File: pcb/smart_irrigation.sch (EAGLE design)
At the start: 31 parts, among them IC1 TMP36, IC2 7805DT, IC3 7833DT, IC4 DS1307, Q1 IRF730, Q2 32.768, Q3 2N3904, U1 BL600

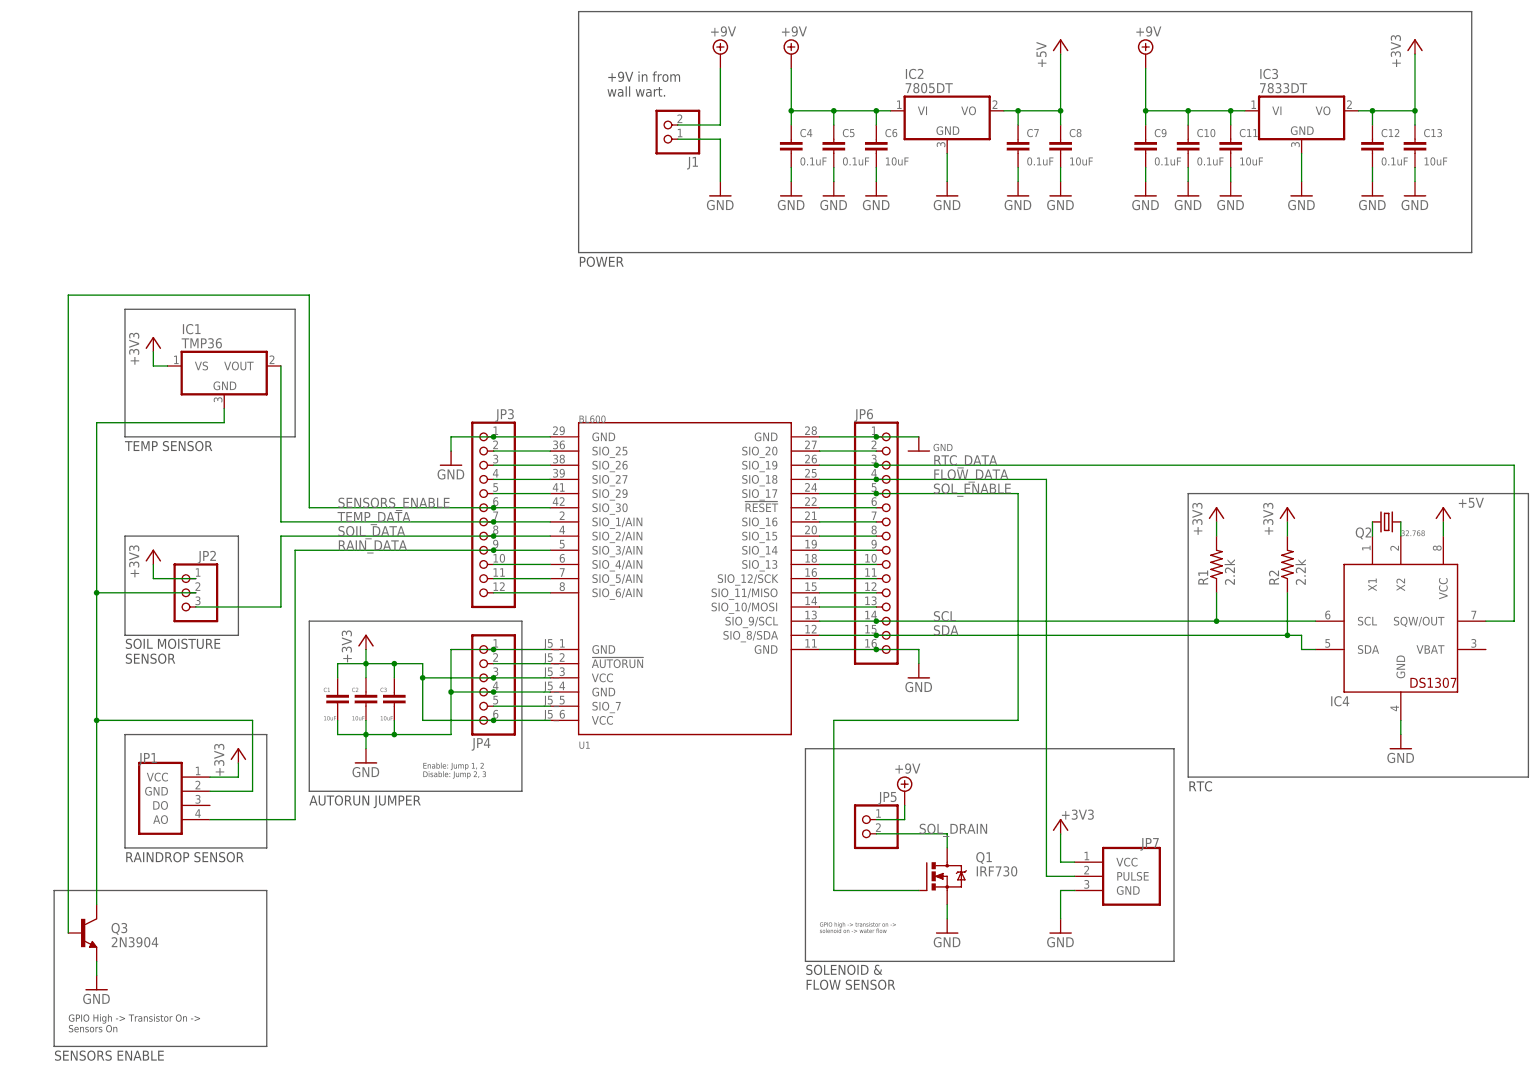
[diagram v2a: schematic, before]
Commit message: PCB: Change flow sensor GPIO pin
The flow sensor's pin was on the opposite side of the other sensors,
making for awkward routing.
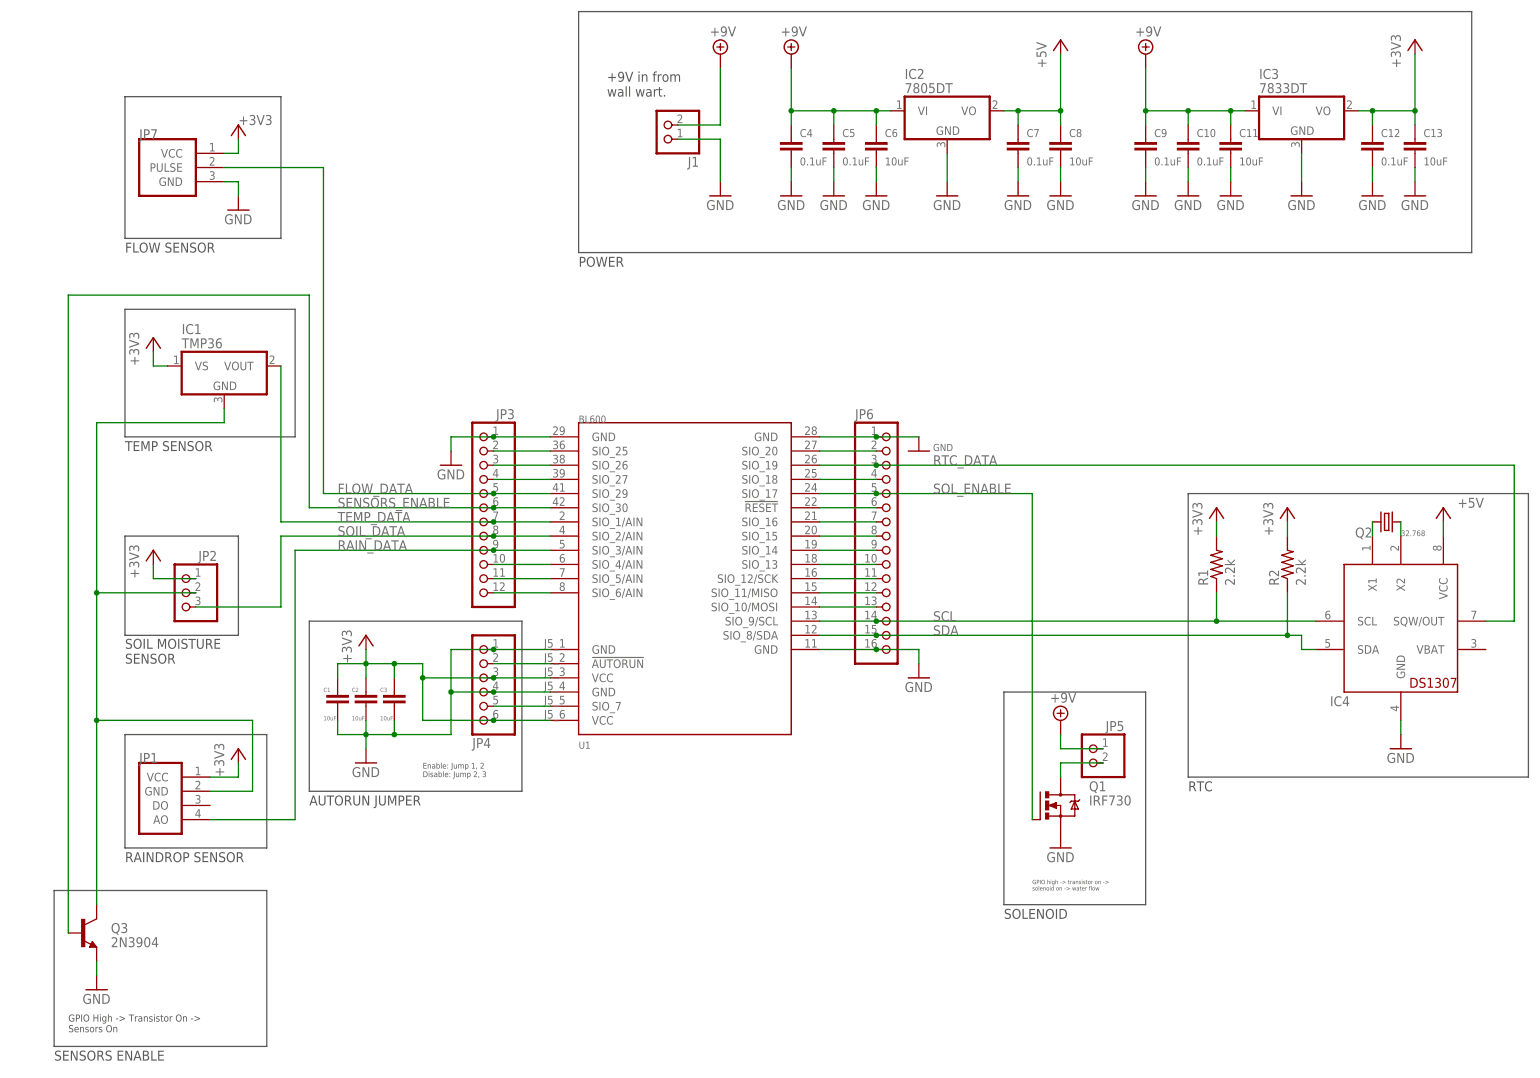
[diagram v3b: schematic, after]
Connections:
- removed net SIO_29: JP3.5, U1.SIO_29
- new net SIO_18: JP6.4, U1.SIO_18
- net FLOW_DATA: now also JP3.5, U1.SIO_29; no longer JP6.4, U1.SIO_18
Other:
- note added: "FLOW SENSOR"
- note added: "SOLENOID"
- note removed: "SOLENOID & FLOW SENSOR"
- moved on the sheet: JP5, JP7, Q1
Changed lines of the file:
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@@
 <setting verticaltext="up"/>
 </settings>
-<grid distance="0.1" unitdist="inch" unit="inch" style="lines" multiple="1" display="no" altdistance="0.01" altunitdist="inch" altunit="inch"/>
+<grid distance="0.1" unitdist="inch" unit="inch" style="lines" multiple="1" display="yes" altdistance="0.01" altunitdist="inch" altunit="inch"/>
 <layers>
 <layer number="1" name="Top" color="4" fill="1" visible="no" active="no"/>
@@
 <wire x1="93.98" y1="68.58" x2="55.88" y2="68.58" width="0.1524" layer="97"/>
 <wire x1="55.88" y1="68.58" x2="55.88" y2="99.06" width="0.1524" layer="97"/>
-<wire x1="144.78" y1="38.1" x2="144.78" y2="76.2" width="0.1524" layer="97"/>
-<wire x1="144.78" y1="76.2" x2="210.82" y2="76.2" width="0.1524" layer="97"/>
-<wire x1="210.82" y1="76.2" x2="210.82" y2="38.1" width="0.1524" layer="97"/>
-<wire x1="210.82" y1="38.1" x2="144.78" y2="38.1" width="0.1524" layer="97"/>
-<text x="144.78" y="33.02" size="1.778" layer="97">SOLENOID &amp;
-FLOW SENSOR</text>
-<text x="147.32" y="43.18" size="0.762" layer="97">GPIO high -&gt; transistor on -&gt;
+<wire x1="180.34" y1="48.26" x2="180.34" y2="86.36" width="0.1524" layer="97"/>
+<wire x1="180.34" y1="86.36" x2="205.74" y2="86.36" width="0.1524" layer="97"/>
+<wire x1="205.74" y1="86.36" x2="205.74" y2="48.26" width="0.1524" layer="97"/>
+<wire x1="205.74" y1="48.26" x2="180.34" y2="48.26" width="0.1524" layer="97"/>
+<text x="180.34" y="45.72" size="1.778" layer="97">SOLENOID</text>
+<text x="185.42" y="50.8" size="0.762" layer="97">GPIO high -&gt; transistor on -&gt;
 solenoid on -&gt; water flow</text>
 <wire x1="10.16" y1="50.8" x2="48.26" y2="50.8" width="0.1524" layer="97"/>
@@
 <text x="12.7" y="25.4" size="1.27" layer="97">GPIO High -&gt; Transistor On -&gt;
 Sensors On</text>
+<wire x1="22.86" y1="193.04" x2="50.8" y2="193.04" width="0.1524" layer="97"/>
+<wire x1="50.8" y1="193.04" x2="50.8" y2="167.64" width="0.1524" layer="97"/>
+<wire x1="50.8" y1="167.64" x2="22.86" y2="167.64" width="0.1524" layer="97"/>
+<wire x1="22.86" y1="167.64" x2="22.86" y2="193.04" width="0.1524" layer="97"/>
+<text x="22.86" y="165.1" size="1.778" layer="97">FLOW SENSOR</text>
 </plain>
 <instances>
@@
 <attribute name="VALUE" x="68.58" y="81.28" size="0.762" layer="96"/>
 </instance>
-<instance part="JP7" gate="A" x="200.66" y="53.34" rot="MR0"/>
-<instance part="+3V35" gate="G$1" x="190.5" y="63.5" smashed="yes">
-<attribute name="VALUE" x="190.5" y="63.5" size="1.778" layer="96"/>
-</instance>
-<instance part="GND14" gate="1" x="190.5" y="43.18"/>
-<instance part="Q1" gate="G$1" x="167.64" y="53.34"/>
-<instance part="JP5" gate="G$1" x="154.94" y="60.96" rot="MR0"/>
-<instance part="SUPPLY3" gate="G$1" x="162.56" y="68.58"/>
-<instance part="GND9" gate="1" x="170.18" y="43.18"/>
+<instance part="JP7" gate="A" x="33.02" y="180.34"/>
+<instance part="+3V35" gate="G$1" x="43.18" y="187.96" smashed="yes">
+<attribute name="VALUE" x="43.18" y="187.96" size="1.778" layer="96"/>
+</instance>
+<instance part="GND14" gate="1" x="43.18" y="172.72"/>
+<instance part="Q1" gate="G$1" x="187.96" y="66.04"/>
+<instance part="JP5" gate="G$1" x="195.58" y="73.66" rot="MR0"/>
+<instance part="SUPPLY3" gate="G$1" x="190.5" y="81.28"/>
+<instance part="GND9" gate="1" x="190.5" y="58.42"/>
 <instance part="Q3" gate="G1" x="15.24" y="43.18" smashed="yes">
 <attribute name="NAME" x="20.32" y="43.18" size="1.778" layer="95"/>
@@
 <pinref part="JP7" gate="A" pin="GND"/>
 <pinref part="GND14" gate="1" pin="GND"/>
-<wire x1="193.04" y1="50.8" x2="190.5" y2="50.8" width="0.1524" layer="91"/>
-<wire x1="190.5" y1="50.8" x2="190.5" y2="45.72" width="0.1524" layer="91"/>
+<wire x1="40.64" y1="177.8" x2="43.18" y2="177.8" width="0.1524" layer="91"/>
+<wire x1="43.18" y1="177.8" x2="43.18" y2="175.26" width="0.1524" layer="91"/>
 </segment>
 <segment>
 <pinref part="GND9" gate="1" pin="GND"/>
 <pinref part="Q1" gate="G$1" pin="S"/>
-<wire x1="170.18" y1="45.72" x2="170.18" y2="48.26" width="0.1524" layer="91"/>
 </segment>
 <segment>
@@
 <segment>
 <pinref part="SUPPLY3" gate="G$1" pin="+9V"/>
-<wire x1="162.56" y1="66.04" x2="162.56" y2="63.5" width="0.1524" layer="91"/>
+<wire x1="190.5" y1="78.74" x2="190.5" y2="76.2" width="0.1524" layer="91"/>
 <pinref part="JP5" gate="G$1" pin="1"/>
-<wire x1="162.56" y1="63.5" x2="157.48" y2="63.5" width="0.1524" layer="91"/>
+<wire x1="190.5" y1="76.2" x2="198.12" y2="76.2" width="0.1524" layer="91"/>
 </segment>
 </net>
@@
 <segment>
 <pinref part="+3V35" gate="G$1" pin="+3V3"/>
-<wire x1="190.5" y1="60.96" x2="190.5" y2="55.88" width="0.1524" layer="91"/>
+<wire x1="43.18" y1="185.42" x2="43.18" y2="182.88" width="0.1524" layer="91"/>
 <pinref part="JP7" gate="A" pin="VCC"/>
-<wire x1="190.5" y1="55.88" x2="193.04" y2="55.88" width="0.1524" layer="91"/>
+<wire x1="43.18" y1="182.88" x2="40.64" y2="182.88" width="0.1524" layer="91"/>
 </segment>
 </net>
@@
 </segment>
 </net>
-<net name="SIO_29" class="0">
+<net name="FLOW_DATA" class="0">
 <segment>
 <pinref part="U1" gate="G$1" pin="SIO_29"/>
 <pinref part="JP3" gate="G$1" pin="5"/>
 <wire x1="99.06" y1="121.92" x2="88.9" y2="121.92" width="0.1524" layer="91"/>
+<pinref part="JP7" gate="A" pin="PULSE"/>
+<wire x1="40.64" y1="180.34" x2="58.42" y2="180.34" width="0.1524" layer="91"/>
+<wire x1="58.42" y1="180.34" x2="58.42" y2="121.92" width="0.1524" layer="91"/>
+<wire x1="58.42" y1="121.92" x2="88.9" y2="121.92" width="0.1524" layer="91"/>
+<junction x="88.9" y="121.92"/>
+<label x="60.96" y="121.92" size="1.778" layer="95"/>
 </segment>
 </net>
@@
 </segment>
 </net>
-<net name="FLOW_DATA" class="0">
-<segment>
-<pinref part="JP6" gate="A" pin="4"/>
-<pinref part="U1" gate="G$1" pin="SIO_18"/>
-<wire x1="157.48" y1="124.46" x2="147.32" y2="124.46" width="0.1524" layer="91"/>
-<pinref part="JP7" gate="A" pin="PULSE"/>
-<wire x1="193.04" y1="53.34" x2="187.96" y2="53.34" width="0.1524" layer="91"/>
-<wire x1="187.96" y1="53.34" x2="187.96" y2="124.46" width="0.1524" layer="91"/>
-<wire x1="187.96" y1="124.46" x2="157.48" y2="124.46" width="0.1524" layer="91"/>
-<junction x="157.48" y="124.46"/>
-<label x="167.64" y="124.46" size="1.778" layer="95"/>
-</segment>
-</net>
 <net name="SOL_ENABLE" class="0">
 <segment>
@@
 <pinref part="JP6" gate="A" pin="5"/>
 <wire x1="147.32" y1="121.92" x2="157.48" y2="121.92" width="0.1524" layer="91"/>
-<wire x1="157.48" y1="121.92" x2="182.88" y2="121.92" width="0.1524" layer="91"/>
-<wire x1="182.88" y1="121.92" x2="182.88" y2="81.28" width="0.1524" layer="91"/>
+<wire x1="157.48" y1="121.92" x2="185.42" y2="121.92" width="0.1524" layer="91"/>
+<wire x1="185.42" y1="121.92" x2="185.42" y2="63.5" width="0.1524" layer="91"/>
 <junction x="157.48" y="121.92"/>
-<wire x1="182.88" y1="81.28" x2="149.86" y2="81.28" width="0.1524" layer="91"/>
-<wire x1="149.86" y1="81.28" x2="149.86" y2="50.8" width="0.1524" layer="91"/>
 <pinref part="Q1" gate="G$1" pin="G"/>
-<wire x1="149.86" y1="50.8" x2="165.1" y2="50.8" width="0.1524" layer="91"/>
 <label x="167.64" y="121.92" size="1.778" layer="95"/>
 </segment>
@@
 <pinref part="JP5" gate="G$1" pin="2"/>
 <pinref part="Q1" gate="G$1" pin="D"/>
-<wire x1="157.48" y1="60.96" x2="170.18" y2="60.96" width="0.1524" layer="91"/>
-<wire x1="170.18" y1="60.96" x2="170.18" y2="58.42" width="0.1524" layer="91"/>
-<label x="165.1" y="60.96" size="1.778" layer="95"/>
+<wire x1="198.12" y1="73.66" x2="190.5" y2="73.66" width="0.1524" layer="91"/>
+<wire x1="190.5" y1="73.66" x2="190.5" y2="71.12" width="0.1524" layer="91"/>
 </segment>
 </net>
@@
 </segment>
 </net>
+<net name="SIO_18" class="0">
+<segment>
+<pinref part="U1" gate="G$1" pin="SIO_18"/>
+<pinref part="JP6" gate="A" pin="4"/>
+<wire x1="157.48" y1="124.46" x2="147.32" y2="124.46" width="0.1524" layer="91"/>
+</segment>
+</net>

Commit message: PCB: Add reset button
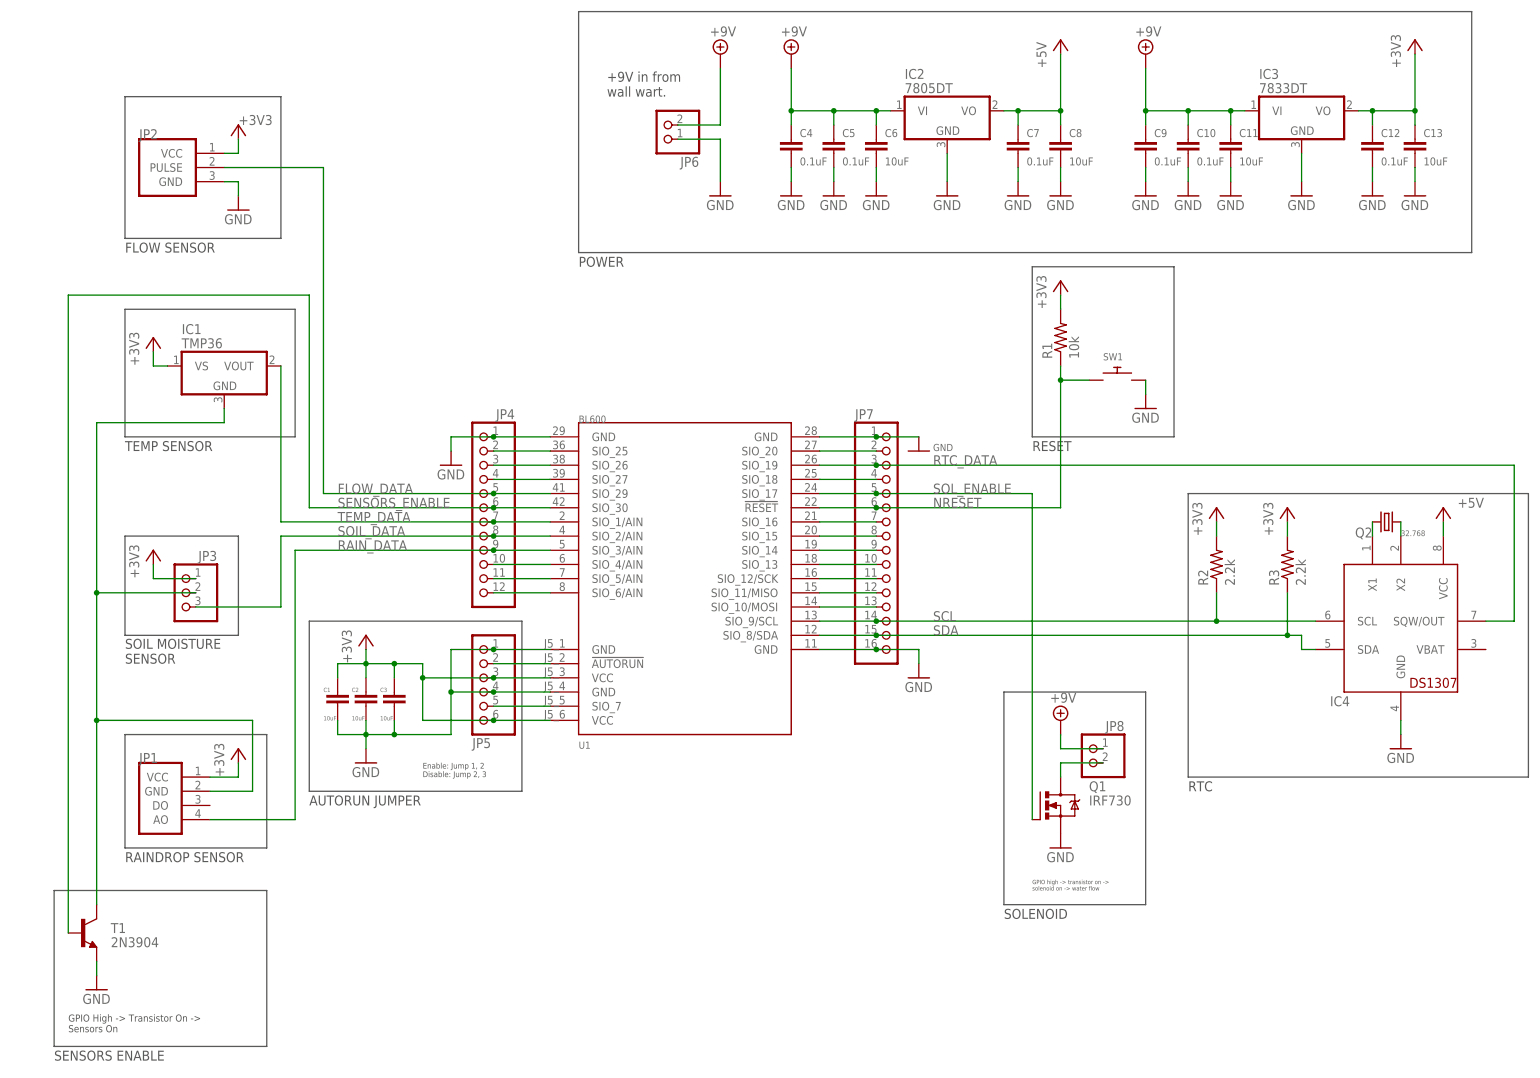
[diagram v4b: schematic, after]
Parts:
- removed J1: (no value), pinhead:PINHD-1X2
- added JP8: (no value), pinhead:PINHD-1X2
- added R3: 2.2k, rcl:R-US_M0805
- added SW1: (no value), adafruit:SWITCH_PUSHBUTTONEVQ-PE
- JP2: device pinhead:PINHD-1X3 -> smart_irrigation:FLOW
- JP3: device pinhead:PINHD-1X12 -> pinhead:PINHD-1X3
- JP4: device pinhead:PINHD-1X6 -> pinhead:PINHD-1X12
- JP5: device pinhead:PINHD-1X2 -> pinhead:PINHD-1X6
- JP6: device pinhead:PINHD-1X16 -> pinhead:PINHD-1X2
- JP7: device smart_irrigation:FLOW -> pinhead:PINHD-1X16
- R1: value 2.2k -> 10k
- renumbered Q3 to T1
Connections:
- net +3V3: now also JP2.VCC, JP3.1, JP5.3, JP5.6, R3.2; no longer JP2.1, JP4.3, JP4.6, JP7.VCC
- net +9V: now also JP6.2, JP8.1; no longer J1.2, JP5.1
- net 3V3_TRAN_COL: now also JP3.2; no longer JP2.2
- net FLOW_DATA: now also JP2.PULSE, JP4.5; no longer JP3.5, JP7.PULSE
- net GND: now also JP2.GND, JP5.1, JP5.4, JP7.1, JP7.16, SW1.P$2; no longer J1.1, JP3.1, JP4.4, JP6.16, JP7.GND
- net NAUTORUN: now also JP5.2; no longer JP4.2
- net NRESET: now also JP7.6, R1.1, SW1.P$1; no longer JP6.6
- net RAIN_DATA: now also JP4.9; no longer JP3.9
- net RTC_DATA: now also JP7.3; no longer JP6.3
- net SCL: now also JP7.14, R2.1; no longer JP6.14, R1.1
- net SDA: now also JP7.15, R3.1; no longer JP6.15, R2.1
- net SENSORS_ENABLE: now also JP4.6; no longer JP3.6
- net SIO_10/MOSI: now also JP7.13; no longer JP6.13
- net SIO_11/MISO: now also JP7.12; no longer JP6.12
- net SIO_12/SCK: now also JP7.11; no longer JP6.11
- net SIO_13: now also JP7.10; no longer JP6.10
- net SIO_14: now also JP7.9; no longer JP6.9
- net SIO_15: now also JP7.8; no longer JP6.8
- net SIO_16: now also JP7.7; no longer JP6.7
- net SIO_18: now also JP7.4; no longer JP6.4
- net SIO_20: now also JP7.2; no longer JP6.2
- net SIO_25: now also JP4.2; no longer JP3.2
- net SIO_26: now also JP4.3; no longer JP3.3
- net SIO_27: now also JP4.4; no longer JP3.4
- net SIO_4: now also JP4.10; no longer JP3.10
- net SIO_5: now also JP4.11; no longer JP3.11
- net SIO_6: now also JP4.12; no longer JP3.12
- net SIO_7: now also JP5.5; no longer JP4.5
- net SOIL_DATA: now also JP3.3, JP4.8; no longer JP2.3, JP3.8
- net SOL_DRAIN: now also JP8.2; no longer JP5.2
- net SOL_ENABLE: now also JP7.5; no longer JP6.5
- net TEMP_DATA: now also JP4.7; no longer JP3.7
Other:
- note added: "RESET"
- moved on the sheet: JP2, R1, R2
